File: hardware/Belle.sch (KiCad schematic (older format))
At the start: 22 parts, among them P1 Bell CONN, P2 Battery CONN, P3 FTDI Flashing CONN, P4 Boot JUMPER, U1 74AHC1G14, U2 ESP-12, U3 AP2112

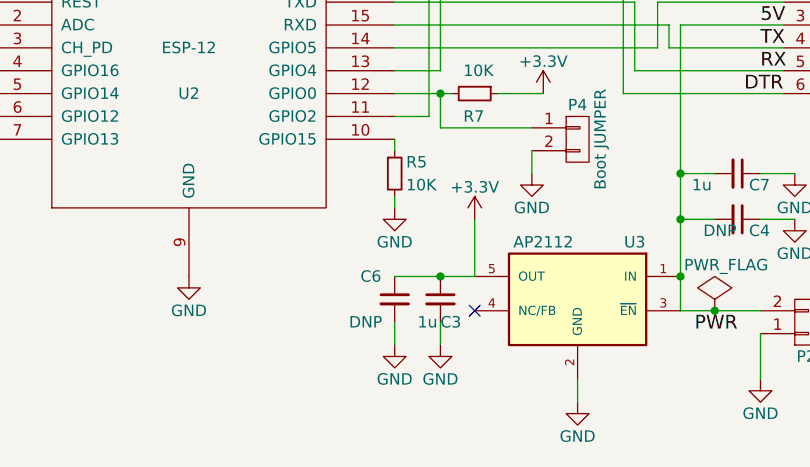
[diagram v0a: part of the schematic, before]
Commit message: add dfm tweaks. #18
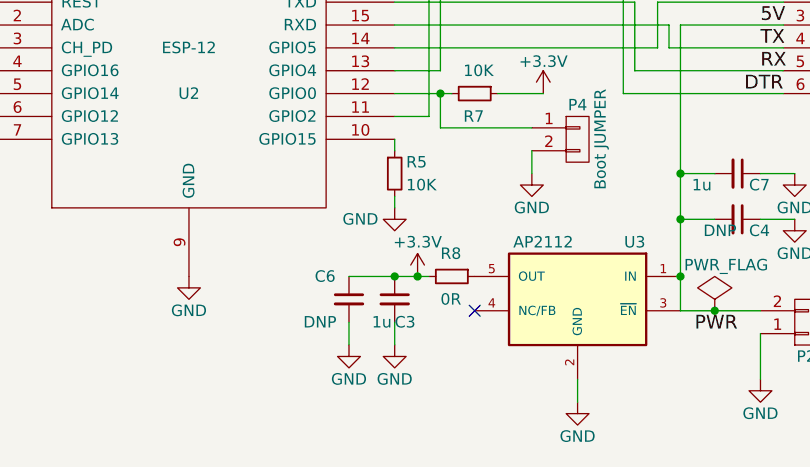
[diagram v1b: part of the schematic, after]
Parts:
- added R8: 0R, symbol R_Small
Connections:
- net +3V3: now also R8.2; no longer U3.5 (OUT)
- new net: R8.1, U3.5 (OUT)
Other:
- moved on the sheet: C3, C6
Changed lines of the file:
@@
 $EndComp
 $Comp
-L GND #PWR01
+L GND #PWR8
 U 1 1 58BBCCFC
 P 5900 4700
-F 0 "#PWR01" H 5900 4450 50  0001 C CNN
+F 0 "#PWR8" H 5900 4450 50  0001 C CNN
 F 1 "GND" H 5900 4550 50  0000 C CNN
 F 2 "" H 5900 4700 50  0000 C CNN
@@
 $EndComp
 $Comp
-L +3.3V #PWR02
+L +3.3V #PWR7
 U 1 1 58BBCD12
 P 5900 2500
-F 0 "#PWR02" H 5900 2350 50  0001 C CNN
+F 0 "#PWR7" H 5900 2350 50  0001 C CNN
 F 1 "+3.3V" H 5900 2640 50  0000 C CNN
 F 2 "" H 5900 2500 50  0000 C CNN
@@
 $EndComp
 $Comp
-L GND #PWR03
+L GND #PWR11
 U 1 1 58BBCDC5
 P 6650 2900
-F 0 "#PWR03" H 6650 2650 50  0001 C CNN
+F 0 "#PWR11" H 6650 2650 50  0001 C CNN
 F 1 "GND" H 6650 2750 50  0000 C CNN
 F 2 "" H 6650 2900 50  0000 C CNN
@@
 $EndComp
 $Comp
-L GND #PWR04
+L GND #PWR5
 U 1 1 58BBD0DA
 P 3600 3800
-F 0 "#PWR04" H 3600 3550 50  0001 C CNN
+F 0 "#PWR5" H 3600 3550 50  0001 C CNN
 F 1 "GND" H 3600 3650 50  0000 C CNN
 F 2 "" H 3600 3800 50  0000 C CNN
@@
 $EndComp
 $Comp
-L +3.3V #PWR05
+L +3.3V #PWR4
 U 1 1 58BBD0F6
 P 3600 3150
-F 0 "#PWR05" H 3600 3000 50  0001 C CNN
+F 0 "#PWR4" H 3600 3000 50  0001 C CNN
 F 1 "+3.3V" H 3600 3290 50  0000 C CNN
 F 2 "" H 3600 3150 50  0000 C CNN
@@
 $EndComp
 $Comp
-L GND #PWR06
+L GND #PWR3
 U 1 1 58BBD1A3
 P 3100 4000
-F 0 "#PWR06" H 3100 3750 50  0001 C CNN
+F 0 "#PWR3" H 3100 3750 50  0001 C CNN
 F 1 "GND" H 3100 3850 50  0000 C CNN
 F 2 "" H 3100 4000 50  0000 C CNN
@@
 $EndComp
 $Comp
-L +3.3V #PWR07
+L +3.3V #PWR1
 U 1 1 58BBD349
 P 2550 3900
-F 0 "#PWR07" H 2550 3750 50  0001 C CNN
+F 0 "#PWR1" H 2550 3750 50  0001 C CNN
 F 1 "+3.3V" H 2550 4040 50  0000 C CNN
 F 2 "" H 2550 3900 50  0000 C CNN
@@
 $EndComp
 $Comp
-L GND #PWR08
+L GND #PWR2
 U 1 1 58BBD44E
 P 2600 3050
-F 0 "#PWR08" H 2600 2800 50  0001 C CNN
+F 0 "#PWR2" H 2600 2800 50  0001 C CNN
 F 1 "GND" H 2600 2900 50  0000 C CNN
 F 2 "" H 2600 3050 50  0000 C CNN
@@
 $EndComp
 $Comp
-L +3.3V #PWR09
+L +3.3V #PWR6
 U 1 1 58BBD4B2
 P 4350 3700
-F 0 "#PWR09" H 4350 3550 50  0001 C CNN
+F 0 "#PWR6" H 4350 3550 50  0001 C CNN
 F 1 "+3.3V" H 4350 3840 50  0000 C CNN
 F 2 "" H 4350 3700 50  0000 C CNN
@@
 $EndComp
 $Comp
-L +3.3V #PWR010
+L +3.3V #PWR17
 U 1 1 58BBD5B6
 P 7450 3900
-F 0 "#PWR010" H 7450 3750 50  0001 C CNN
+F 0 "#PWR17" H 7450 3750 50  0001 C CNN
 F 1 "+3.3V" H 7450 4040 50  0000 C CNN
 F 2 "" H 7450 3900 50  0000 C CNN
@@
 $EndComp
 $Comp
-L GND #PWR011
+L GND #PWR12
 U 1 1 58BBD6CB
 P 6800 4400
-F 0 "#PWR011" H 6800 4150 50  0001 C CNN
-F 1 "GND" H 6800 4250 50  0000 C CNN
+F 0 "#PWR12" H 6800 4150 50  0001 C CNN
+F 1 "GND" H 6650 4350 50  0000 C CNN
 F 2 "" H 6800 4400 50  0000 C CNN
 F 3 "" H 6800 4400 50  0000 C CNN
@@
 $EndComp
 $Comp
-L +3.3V #PWR012
+L +3.3V #PWR14
 U 1 1 58BBDA6C
-P 7150 4450
-F 0 "#PWR012" H 7150 4300 50  0001 C CNN
-F 1 "+3.3V" H 7150 4590 50  0000 C CNN
-F 2 "" H 7150 4450 50  0000 C CNN
-F 3 "" H 7150 4450 50  0000 C CNN
-	1    7150 4450
+P 6900 4700
+F 0 "#PWR14" H 6900 4550 50  0001 C CNN
+F 1 "+3.3V" H 6900 4850 50  0000 C CNN
+F 2 "" H 6900 4700 50  0000 C CNN
+F 3 "" H 6900 4700 50  0000 C CNN
+	1    6900 4700
 	-1   0    0    -1
 $EndComp
@@
 $EndComp
 $Comp
-L GND #PWR013
+L GND #PWR18
 U 1 1 58BBDB81
 P 7600 5250
-F 0 "#PWR013" H 7600 5000 50  0001 C CNN
+F 0 "#PWR18" H 7600 5000 50  0001 C CNN
 F 1 "GND" H 7600 5100 50  0000 C CNN
 F 2 "" H 7600 5250 50  0000 C CNN
@@
 $EndComp
 $Comp
-L GND #PWR014
+L GND #PWR20
 U 1 1 58BBDD34
 P 8400 5150
-F 0 "#PWR014" H 8400 4900 50  0001 C CNN
+F 0 "#PWR20" H 8400 4900 50  0001 C CNN
 F 1 "GND" H 8400 5000 50  0000 C CNN
 F 2 "" H 8400 5150 50  0000 C CNN
@@
 $EndComp
 $Comp
-L GND #PWR015
+L GND #PWR19
 U 1 1 58BBDF88
 P 8100 3000
-F 0 "#PWR015" H 8100 2750 50  0001 C CNN
+F 0 "#PWR19" H 8100 2750 50  0001 C CNN
 F 1 "GND" H 8100 2850 50  0000 C CNN
 F 2 "" H 8100 3000 50  0000 C CNN
@@
 $EndComp
 $Comp
-L +3.3V #PWR016
+L +3.3V #PWR15
 U 1 1 58BBED05
 P 6950 2650
-F 0 "#PWR016" H 6950 2500 50  0001 C CNN
+F 0 "#PWR15" H 6950 2500 50  0001 C CNN
 F 1 "+3.3V" H 6950 2800 50  0000 C CNN
 F 2 "" H 6950 2650 50  0000 C CNN
@@
 NoConn ~ 7150 4850
 $Comp
-L PWR_FLAG #FLG017
+L PWR_FLAG #FLG1
 U 1 1 58BBEBAB
 P 8200 4850
-F 0 "#FLG017" H 8200 4945 50  0001 C CNN
+F 0 "#FLG1" H 8200 4945 50  0001 C CNN
 F 1 "PWR_FLAG" H 8250 5050 50  0000 C CNN
 F 2 "" H 8200 4850 50  0000 C CNN
@@
 $EndComp
 $Comp
-L GND #PWR018
+L GND #PWR22
 U 1 1 58CE4ED3
 P 8550 4450
-F 0 "#PWR018" H 8550 4200 50  0001 C CNN
+F 0 "#PWR22" H 8550 4200 50  0001 C CNN
 F 1 "GND" H 8550 4300 50  0000 C CNN
 F 2 "" H 8550 4450 50  0000 C CNN
@@
 L C_Small C3
 U 1 1 58CE500B
-P 7000 4800
-F 0 "C3" H 7000 4700 50  0000 L CNN
-F 1 "1u" H 6900 4700 50  0000 L CNN
-F 2 "Capacitors_SMD:C_1206_HandSoldering" H 7000 4800 50  0001 C CNN
-F 3 "" H 7000 4800 50  0000 C CNN
-	1    7000 4800
-	1    0    0    -1
-$EndComp
-$Comp
-L GND #PWR019
+P 6800 4800
+F 0 "C3" H 6800 4700 50  0000 L CNN
+F 1 "1u" H 6700 4700 50  0000 L CNN
+F 2 "Capacitors_SMD:C_1206_HandSoldering" H 6800 4800 50  0001 C CNN
+F 3 "" H 6800 4800 50  0000 C CNN
+	1    6800 4800
+	1    0    0    -1
+$EndComp
+$Comp
+L GND #PWR9
 U 1 1 58CE504A
-P 6800 5000
-F 0 "#PWR019" H 6800 4750 50  0001 C CNN
-F 1 "GND" H 6800 4850 50  0000 C CNN
-F 2 "" H 6800 5000 50  0000 C CNN
-F 3 "" H 6800 5000 50  0000 C CNN
-	1    6800 5000
+P 6600 5000
+F 0 "#PWR9" H 6600 4750 50  0001 C CNN
+F 1 "GND" H 6600 4850 50  0000 C CNN
+F 2 "" H 6600 5000 50  0000 C CNN
+F 3 "" H 6600 5000 50  0000 C CNN
+	1    6600 5000
 	1    0    0    -1
 $EndComp
@@
 	6800 4350 6800 4400
 Wire Wire Line
-	7150 4700 7150 4450
-Wire Wire Line
 	7600 5150 7600 5250
 Wire Wire Line
@@
 	4700 2900 4700 3000
 Connection ~ 5900 2900
-Wire Wire Line
-	6800 4900 6800 5000
 Wire Notes Line
 	2700 3300 3250 3300
@@
 Connection ~ 5900 2550
 $Comp
-L GND #PWR020
+L GND #PWR10
 U 1 1 59070D65
 P 6650 2550
-F 0 "#PWR020" H 6650 2300 50  0001 C CNN
+F 0 "#PWR10" H 6650 2300 50  0001 C CNN
 F 1 "GND" H 6650 2400 50  0000 C CNN
 F 2 "" H 6650 2550 50  0000 C CNN
@@
 	8400 4450 8550 4450
 $Comp
-L GND #PWR021
+L GND #PWR21
 U 1 1 59071152
 P 8550 4250
-F 0 "#PWR021" H 8550 4000 50  0001 C CNN
+F 0 "#PWR21" H 8550 4000 50  0001 C CNN
 F 1 "GND" H 8550 4100 50  0000 C CNN
 F 2 "" H 8550 4250 50  0000 C CNN
@@
 L C_Small C6
 U 1 1 590712F7
-P 6800 4800
-F 0 "C6" H 6650 4900 50  0000 L CNN
-F 1 "DNP" H 6600 4700 50  0000 L CNN
-F 2 "Capacitors_SMD:C_1206_HandSoldering" H 6800 4800 50  0001 C CNN
-F 3 "" H 6800 4800 50  0000 C CNN
-	1    6800 4800
-	1    0    0    -1
-$EndComp
-$Comp
-L GND #PWR022
+P 6600 4800
+F 0 "C6" H 6450 4900 50  0000 L CNN
+F 1 "DNP" H 6400 4700 50  0000 L CNN
+F 2 "Capacitors_SMD:C_1206_HandSoldering" H 6600 4800 50  0001 C CNN
+F 3 "" H 6600 4800 50  0000 C CNN
+	1    6600 4800
+	1    0    0    -1
+$EndComp
+$Comp
+L GND #PWR13
 U 1 1 5907137C
-P 7000 5000
-F 0 "#PWR022" H 7000 4750 50  0001 C CNN
-F 1 "GND" H 7000 4850 50  0000 C CNN
-F 2 "" H 7000 5000 50  0000 C CNN
-F 3 "" H 7000 5000 50  0000 C CNN
-	1    7000 5000
-	1    0    0    -1
-$EndComp
-Wire Wire Line
-	7000 4900 7000 5000
-Wire Wire Line
-	6800 4700 7150 4700
-Connection ~ 7000 4700
+P 6800 5000
+F 0 "#PWR13" H 6800 4750 50  0001 C CNN
+F 1 "GND" H 6800 4850 50  0000 C CNN
+F 2 "" H 6800 5000 50  0000 C CNN
+F 3 "" H 6800 5000 50  0000 C CNN
+	1    6800 5000
+	1    0    0    -1
+$EndComp
 Wire Wire Line
 	6950 4000 6950 3050
@@
 Connection ~ 7000 3900
 $Comp
-L GND #PWR023
+L GND #PWR16
 U 1 1 59074532
 P 7400 4250
-F 0 "#PWR023" H 7400 4000 50  0001 C CNN
+F 0 "#PWR16" H 7400 4000 50  0001 C CNN
 F 1 "GND" H 7400 4100 50  0000 C CNN
 F 2 "" H 7400 4250 50  0000 C CNN
@@
 Wire Wire Line
 	7800 3900 8500 3900
+$Comp
+L R_Small R8
+U 1 1 5912943F
+P 7050 4700
+F 0 "R8" V 6950 4650 50  0000 L CNN
+F 1 "0R" V 7150 4650 50  0000 L CNN
+F 2 "" H 7050 4700 50  0000 C CNN
+F 3 "" H 7050 4700 50  0000 C CNN
+	1    7050 4700
+	0    1    1    0
+$EndComp
+Wire Wire Line
+	6600 4700 6950 4700
+Connection ~ 6800 4700
+Wire Wire Line
+	6600 4900 6600 5000
+Wire Wire Line
+	6800 4900 6800 5000
+Connection ~ 6900 4700
 $EndSCHEMATC

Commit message: modifiec PCB
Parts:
- R8: footprint (none) -> Resistors_SMD:R_1206_HandSoldering
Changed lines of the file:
@@
 $EndComp
 $Comp
-L GND #PWR8
+L GND #PWR01
 U 1 1 58BBCCFC
 P 5900 4700
-F 0 "#PWR8" H 5900 4450 50  0001 C CNN
+F 0 "#PWR01" H 5900 4450 50  0001 C CNN
 F 1 "GND" H 5900 4550 50  0000 C CNN
 F 2 "" H 5900 4700 50  0000 C CNN
@@
 $EndComp
 $Comp
-L +3.3V #PWR7
+L +3.3V #PWR02
 U 1 1 58BBCD12
 P 5900 2500
-F 0 "#PWR7" H 5900 2350 50  0001 C CNN
+F 0 "#PWR02" H 5900 2350 50  0001 C CNN
 F 1 "+3.3V" H 5900 2640 50  0000 C CNN
 F 2 "" H 5900 2500 50  0000 C CNN
@@
 $EndComp
 $Comp
-L GND #PWR11
+L GND #PWR03
 U 1 1 58BBCDC5
 P 6650 2900
-F 0 "#PWR11" H 6650 2650 50  0001 C CNN
+F 0 "#PWR03" H 6650 2650 50  0001 C CNN
 F 1 "GND" H 6650 2750 50  0000 C CNN
 F 2 "" H 6650 2900 50  0000 C CNN
@@
 $EndComp
 $Comp
-L GND #PWR5
+L GND #PWR04
 U 1 1 58BBD0DA
 P 3600 3800
-F 0 "#PWR5" H 3600 3550 50  0001 C CNN
+F 0 "#PWR04" H 3600 3550 50  0001 C CNN
 F 1 "GND" H 3600 3650 50  0000 C CNN
 F 2 "" H 3600 3800 50  0000 C CNN
@@
 $EndComp
 $Comp
-L +3.3V #PWR4
+L +3.3V #PWR05
 U 1 1 58BBD0F6
 P 3600 3150
-F 0 "#PWR4" H 3600 3000 50  0001 C CNN
+F 0 "#PWR05" H 3600 3000 50  0001 C CNN
 F 1 "+3.3V" H 3600 3290 50  0000 C CNN
 F 2 "" H 3600 3150 50  0000 C CNN
@@
 $EndComp
 $Comp
-L GND #PWR3
+L GND #PWR06
 U 1 1 58BBD1A3
 P 3100 4000
-F 0 "#PWR3" H 3100 3750 50  0001 C CNN
+F 0 "#PWR06" H 3100 3750 50  0001 C CNN
 F 1 "GND" H 3100 3850 50  0000 C CNN
 F 2 "" H 3100 4000 50  0000 C CNN
@@
 $EndComp
 $Comp
-L +3.3V #PWR1
+L +3.3V #PWR07
 U 1 1 58BBD349
 P 2550 3900
-F 0 "#PWR1" H 2550 3750 50  0001 C CNN
+F 0 "#PWR07" H 2550 3750 50  0001 C CNN
 F 1 "+3.3V" H 2550 4040 50  0000 C CNN
 F 2 "" H 2550 3900 50  0000 C CNN
@@
 $EndComp
 $Comp
-L GND #PWR2
+L GND #PWR08
 U 1 1 58BBD44E
 P 2600 3050
-F 0 "#PWR2" H 2600 2800 50  0001 C CNN
+F 0 "#PWR08" H 2600 2800 50  0001 C CNN
 F 1 "GND" H 2600 2900 50  0000 C CNN
 F 2 "" H 2600 3050 50  0000 C CNN
@@
 $EndComp
 $Comp
-L +3.3V #PWR6
+L +3.3V #PWR09
 U 1 1 58BBD4B2
 P 4350 3700
-F 0 "#PWR6" H 4350 3550 50  0001 C CNN
+F 0 "#PWR09" H 4350 3550 50  0001 C CNN
 F 1 "+3.3V" H 4350 3840 50  0000 C CNN
 F 2 "" H 4350 3700 50  0000 C CNN
@@
 $EndComp
 $Comp
-L +3.3V #PWR17
+L +3.3V #PWR010
 U 1 1 58BBD5B6
 P 7450 3900
-F 0 "#PWR17" H 7450 3750 50  0001 C CNN
+F 0 "#PWR010" H 7450 3750 50  0001 C CNN
 F 1 "+3.3V" H 7450 4040 50  0000 C CNN
 F 2 "" H 7450 3900 50  0000 C CNN
@@
 $EndComp
 $Comp
-L GND #PWR12
+L GND #PWR011
 U 1 1 58BBD6CB
 P 6800 4400
-F 0 "#PWR12" H 6800 4150 50  0001 C CNN
+F 0 "#PWR011" H 6800 4150 50  0001 C CNN
 F 1 "GND" H 6650 4350 50  0000 C CNN
 F 2 "" H 6800 4400 50  0000 C CNN
@@
 $EndComp
 $Comp
-L +3.3V #PWR14
+L +3.3V #PWR012
 U 1 1 58BBDA6C
 P 6900 4700
-F 0 "#PWR14" H 6900 4550 50  0001 C CNN
+F 0 "#PWR012" H 6900 4550 50  0001 C CNN
 F 1 "+3.3V" H 6900 4850 50  0000 C CNN
 F 2 "" H 6900 4700 50  0000 C CNN
@@
 $EndComp
 $Comp
-L GND #PWR18
+L GND #PWR013
 U 1 1 58BBDB81
 P 7600 5250
-F 0 "#PWR18" H 7600 5000 50  0001 C CNN
+F 0 "#PWR013" H 7600 5000 50  0001 C CNN
 F 1 "GND" H 7600 5100 50  0000 C CNN
 F 2 "" H 7600 5250 50  0000 C CNN
@@
 $EndComp
 $Comp
-L GND #PWR20
+L GND #PWR014
 U 1 1 58BBDD34
 P 8400 5150
-F 0 "#PWR20" H 8400 4900 50  0001 C CNN
+F 0 "#PWR014" H 8400 4900 50  0001 C CNN
 F 1 "GND" H 8400 5000 50  0000 C CNN
 F 2 "" H 8400 5150 50  0000 C CNN
@@
 $EndComp
 $Comp
-L GND #PWR19
+L GND #PWR015
 U 1 1 58BBDF88
 P 8100 3000
-F 0 "#PWR19" H 8100 2750 50  0001 C CNN
+F 0 "#PWR015" H 8100 2750 50  0001 C CNN
 F 1 "GND" H 8100 2850 50  0000 C CNN
 F 2 "" H 8100 3000 50  0000 C CNN
@@
 $EndComp
 $Comp
-L +3.3V #PWR15
+L +3.3V #PWR016
 U 1 1 58BBED05
 P 6950 2650
-F 0 "#PWR15" H 6950 2500 50  0001 C CNN
+F 0 "#PWR016" H 6950 2500 50  0001 C CNN
 F 1 "+3.3V" H 6950 2800 50  0000 C CNN
 F 2 "" H 6950 2650 50  0000 C CNN
@@
 NoConn ~ 7150 4850
 $Comp
-L PWR_FLAG #FLG1
+L PWR_FLAG #FLG017
 U 1 1 58BBEBAB
 P 8200 4850
-F 0 "#FLG1" H 8200 4945 50  0001 C CNN
+F 0 "#FLG017" H 8200 4945 50  0001 C CNN
 F 1 "PWR_FLAG" H 8250 5050 50  0000 C CNN
 F 2 "" H 8200 4850 50  0000 C CNN
@@
 $EndComp
 $Comp
-L GND #PWR22
+L GND #PWR018
 U 1 1 58CE4ED3
 P 8550 4450
-F 0 "#PWR22" H 8550 4200 50  0001 C CNN
+F 0 "#PWR018" H 8550 4200 50  0001 C CNN
 F 1 "GND" H 8550 4300 50  0000 C CNN
 F 2 "" H 8550 4450 50  0000 C CNN
@@
 $EndComp
 $Comp
-L GND #PWR9
+L GND #PWR019
 U 1 1 58CE504A
 P 6600 5000
-F 0 "#PWR9" H 6600 4750 50  0001 C CNN
+F 0 "#PWR019" H 6600 4750 50  0001 C CNN
 F 1 "GND" H 6600 4850 50  0000 C CNN
 F 2 "" H 6600 5000 50  0000 C CNN
@@
 Connection ~ 5900 2550
 $Comp
-L GND #PWR10
+L GND #PWR020
 U 1 1 59070D65
 P 6650 2550
-F 0 "#PWR10" H 6650 2300 50  0001 C CNN
+F 0 "#PWR020" H 6650 2300 50  0001 C CNN
 F 1 "GND" H 6650 2400 50  0000 C CNN
 F 2 "" H 6650 2550 50  0000 C CNN
@@
 	8400 4450 8550 4450
 $Comp
-L GND #PWR21
+L GND #PWR021
 U 1 1 59071152
 P 8550 4250
-F 0 "#PWR21" H 8550 4000 50  0001 C CNN
+F 0 "#PWR021" H 8550 4000 50  0001 C CNN
 F 1 "GND" H 8550 4100 50  0000 C CNN
 F 2 "" H 8550 4250 50  0000 C CNN
@@
 $EndComp
 $Comp
-L GND #PWR13
+L GND #PWR022
 U 1 1 5907137C
 P 6800 5000
-F 0 "#PWR13" H 6800 4750 50  0001 C CNN
+F 0 "#PWR022" H 6800 4750 50  0001 C CNN
 F 1 "GND" H 6800 4850 50  0000 C CNN
 F 2 "" H 6800 5000 50  0000 C CNN
@@
 Connection ~ 7000 3900
 $Comp
-L GND #PWR16
+L GND #PWR023
 U 1 1 59074532
 P 7400 4250
-F 0 "#PWR16" H 7400 4000 50  0001 C CNN
+F 0 "#PWR023" H 7400 4000 50  0001 C CNN
 F 1 "GND" H 7400 4100 50  0000 C CNN
 F 2 "" H 7400 4250 50  0000 C CNN
@@
 F 0 "R8" V 6950 4650 50  0000 L CNN
 F 1 "0R" V 7150 4650 50  0000 L CNN
-F 2 "" H 7050 4700 50  0000 C CNN
+F 2 "Resistors_SMD:R_1206_HandSoldering" H 7050 4700 50  0001 C CNN
 F 3 "" H 7050 4700 50  0000 C CNN
 	1    7050 4700

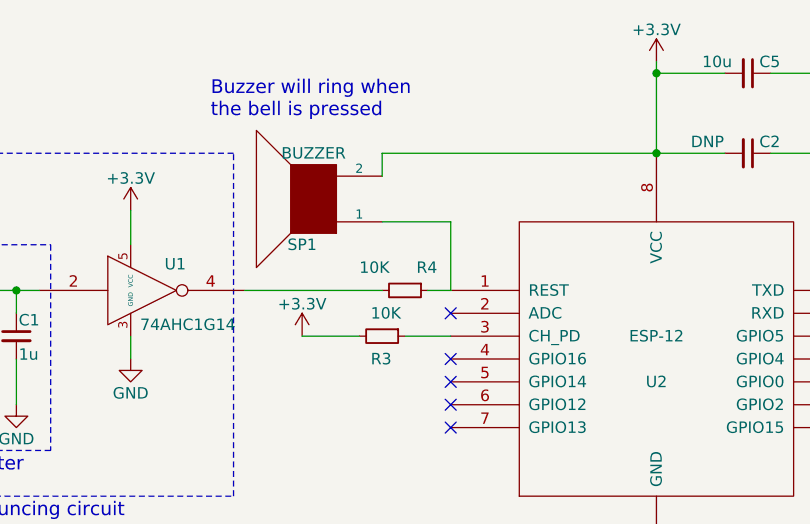
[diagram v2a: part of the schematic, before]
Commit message: add 3 0Ω resistors to schematic and bom
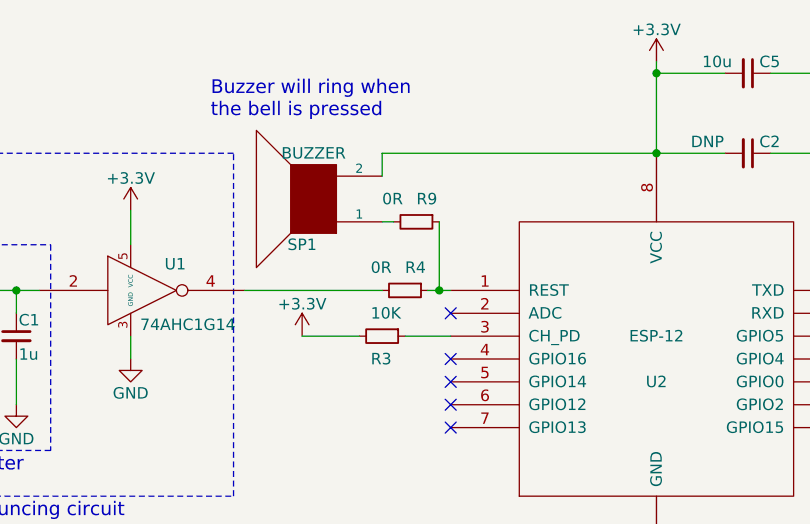
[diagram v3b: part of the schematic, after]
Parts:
- added R9: 0R, symbol R_Small
- R4: value 10K -> 0R
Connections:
- net at R4.1, U2.1 (REST): now also R9.1; no longer SP1.1
- new net: R9.2, SP1.1
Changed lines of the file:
@@
 RC filter
-Wire Wire Line
-	4700 3200 5000 3200
-Wire Wire Line
-	5000 3200 5000 3500
 Wire Wire Line
 	3600 3150 3600 3300
@@
 U 1 1 58FE989D
 P 4800 3500
-F 0 "R4" V 4700 3550 50  0000 L CNN
-F 1 "10K" V 4700 3300 50  0000 L CNN
+F 0 "R4" V 4700 3500 50  0000 L CNN
+F 1 "0R" V 4700 3350 50  0000 L CNN
 F 2 "Resistors_SMD:R_1206_HandSoldering" H 4800 3500 50  0001 C CNN
 F 3 "" H 4800 3500 50  0000 C CNN
@@
 	6800 4900 6800 5000
 Connection ~ 6900 4700
+$Comp
+L R_Small R9
+U 1 1 59937CCF
+P 4850 3200
+F 0 "R9" V 4750 3200 50  0000 L CNN
+F 1 "0R" V 4750 3050 50  0000 L CNN
+F 2 "" H 4850 3200 50  0000 C CNN
+F 3 "" H 4850 3200 50  0000 C CNN
+	1    4850 3200
+	0    1    1    0
+$EndComp
+Wire Wire Line
+	4950 3200 4950 3500
+Connection ~ 4950 3500
+Wire Wire Line
+	4750 3200 4700 3200
 $EndSCHEMATC

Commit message: Save KiCad
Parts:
- R9: footprint (none) -> Resistors_SMD:R_1206_HandSoldering
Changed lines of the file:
@@
 F 0 "R9" V 4750 3200 50  0000 L CNN
 F 1 "0R" V 4750 3050 50  0000 L CNN
-F 2 "" H 4850 3200 50  0000 C CNN
+F 2 "Resistors_SMD:R_1206_HandSoldering" H 4850 3200 50  0001 C CNN
 F 3 "" H 4850 3200 50  0000 C CNN
 	1    4850 3200

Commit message: Save KiCad project
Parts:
- U2: footprint ESP8266:ESP-12 -> ESP-12F-SMD:ESP-12F-SMD
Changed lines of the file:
@@
 F 0 "U2" H 5900 3700 50  0000 C CNN
 F 1 "ESP-12" H 5900 3900 50  0000 C CNN
-F 2 "ESP8266:ESP-12" H 5900 3800 50  0001 C CNN
+F 2 "ESP-12F-SMD:ESP-12F-SMD" H 5900 3800 50  0001 C CNN
 F 3 "" H 5900 3800 50  0001 C CNN
 	1    5900 3800
